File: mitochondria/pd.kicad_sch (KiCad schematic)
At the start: 0 parts

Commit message: Added Samac (Mouser components) & 5V Power distribution
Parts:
- added C? (x3): 15u, symbol Device:C_Polarized
- added C? (x2): 180u, symbol Device:C_Polarized
- added C?: 0.47u, symbol Device:C
- added C?: 0.01u, symbol Device:C
- added D1: VS-6TQ045S-M3, VS6TQ045SM3, symbol SamacSys_Parts:VS-6TQ045S-M3
- added L?: 22uH, symbol Device:L
- added U?: LM2678S-5.0, LM2678S-5.0:TO127P1435X464-8N, symbol mc_Symbols:LM2678S-5.0
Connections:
- new net: C?.2, L?.1, U?.1 (SW)
- new net: C?.1, U?.3 (BOOST)
- new net +5V: C?.1, C?.1, L?.2, U?.6 (FB)
- new net +BATT: C?.1, C?.1, C?.1, C?.1, U?.2 (VIN)
- new net -BATT: C?.2, C?.2, C?.2, C?.2, C?.2, C?.2, D1.3 (A), U?.4 (GND), U?.8 (GND)

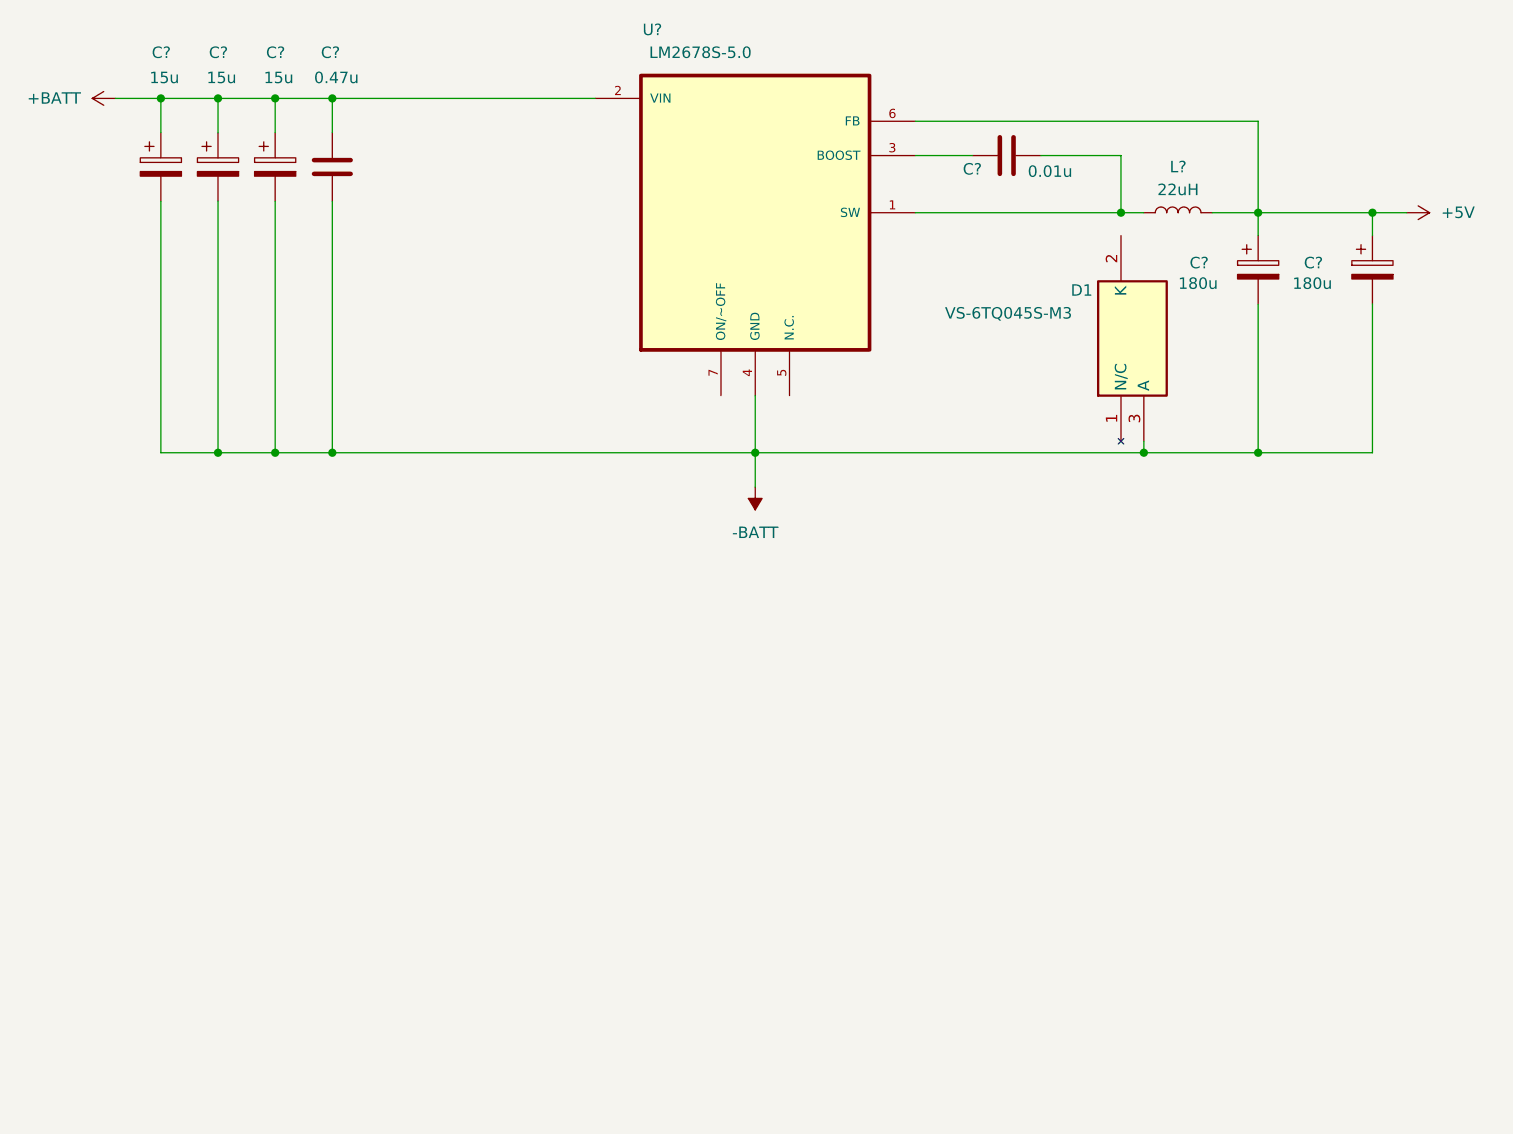
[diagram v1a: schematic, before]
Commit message: Added 12V DCDC, GPIO connection, related components to library
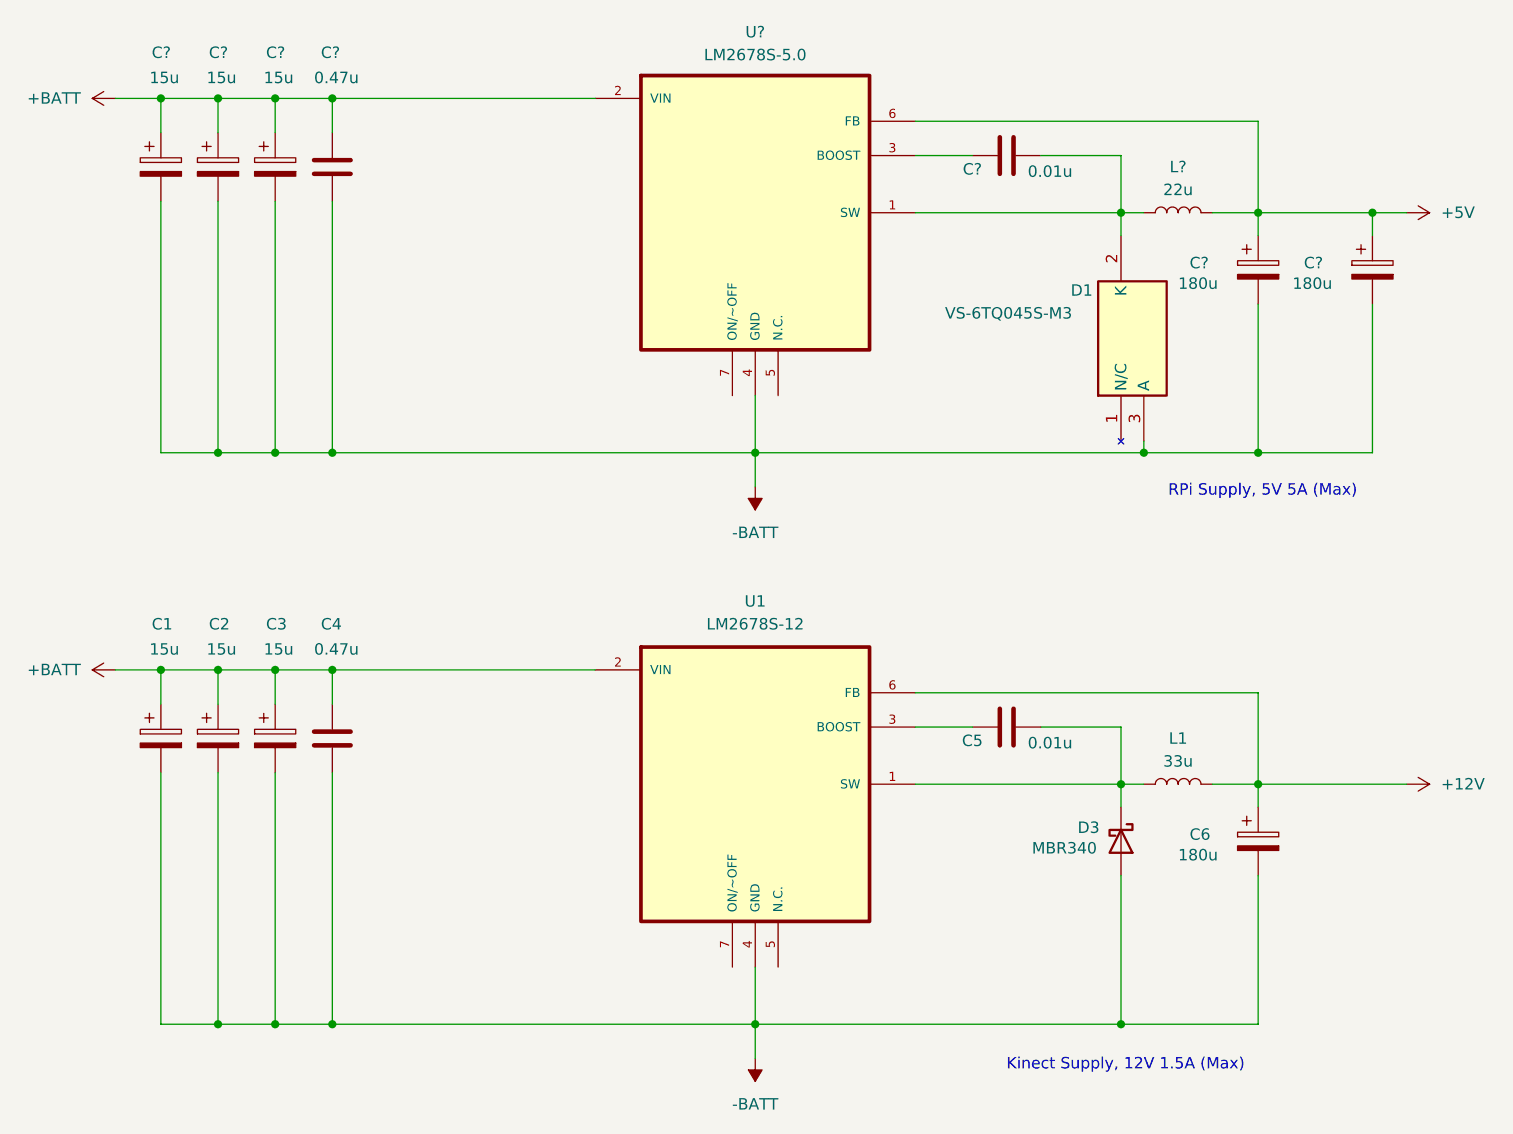
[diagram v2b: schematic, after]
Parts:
- added C1, C2, C3: 15u, symbol Device:C_Polarized
- added C4: 0.47u, symbol Device:C
- added C5: 0.01u, symbol Device:C
- added C6: 180u, symbol Device:C_Polarized
- added D3: MBR340, Diode_THT:D_DO-201AD_P15.24mm_Horizontal, symbol Diode:MBR340
- added L1: 33u, symbol Device:L
- added U1: LM2678S-12, LM2678S-12:TO127P1435X464-8N, symbol mc_Symbols:LM2678S-12
- L?: value 22uH -> 22u
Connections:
- net +BATT: now also C1.1, C2.1, C3.1, C4.1, U1.2 (VIN)
- net -BATT: now also C1.2, C2.2, C3.2, C4.2, C6.2, D3.2 (A), U1.4 (GND), U1.8 (GND)
- net at D1.2 (K): now also C?.2, L?.1, U?.1 (SW)
- new net: C5.2, D3.1 (K), L1.1, U1.1 (SW)
- new net: C5.1, U1.3 (BOOST)
- new net +12V: C6.1, L1.2, U1.6 (FB)
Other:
- note added: "Kinect Supply, 12V 1.5A (Max)"
- note added: "RPi Supply, 5V 5A (Max)"
